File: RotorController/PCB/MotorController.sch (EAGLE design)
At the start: 18 parts

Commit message: Added thermal warning logic and fixed some layout issues.
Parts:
- removed D1: (no value), SparkFun-LED:LED-3MM-NO_SILK
- removed U1: (no value), SparkFun-IC-Power:V_REG_78XX-TO-220
- added IC1: 74ALS02N, 74xx-us:74ALS02N
- added J1: Waring LED, SparkFun-Connectors:CONN_02
- added J2: Power LED, SparkFun-Connectors:CONN_02
- added R10, R8: 2.2K, SparkFun-Resistors:RESISTORAXIAL-0.3
- added R6: 1K, SparkFun-Resistors:RESISTORAXIAL-0.3
- added R7, R9: 3.3K, SparkFun-Resistors:RESISTORAXIAL-0.3
- added U2: 5V, SparkFun-IC-Power:V_REG_78XXSINK
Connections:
- new net AZFLAG: AZHBRIDGE.THERMAL, R7.2
- new net ELFLAG: ELHBRIDGE.THERMAL, R9.2
- new net N$3: IC1D.I1, R10.2, R9.1
- new net N$5: J1.1, R6.2
- new net N$7: IC1D.I0, R7.1, R8.2
- new net WARNINGFLAG: IC1D.O, R6.1, UC1.A0
- net GND: now also IC1A.I0, IC1A.I1, IC1B.I0, IC1B.I1, IC1C.I0, IC1C.I1, IC1P.GND, J1.2, J2.2, R10.1, R8.1, U2.GND; no longer D1.C, U1.GND
- net N$8: now also J2.1; no longer D1.A
- net VCC: now also IC1P.VCC, U2.OUT; no longer U1.OUT
- net VCC_2: now also U2.IN; no longer U1.IN

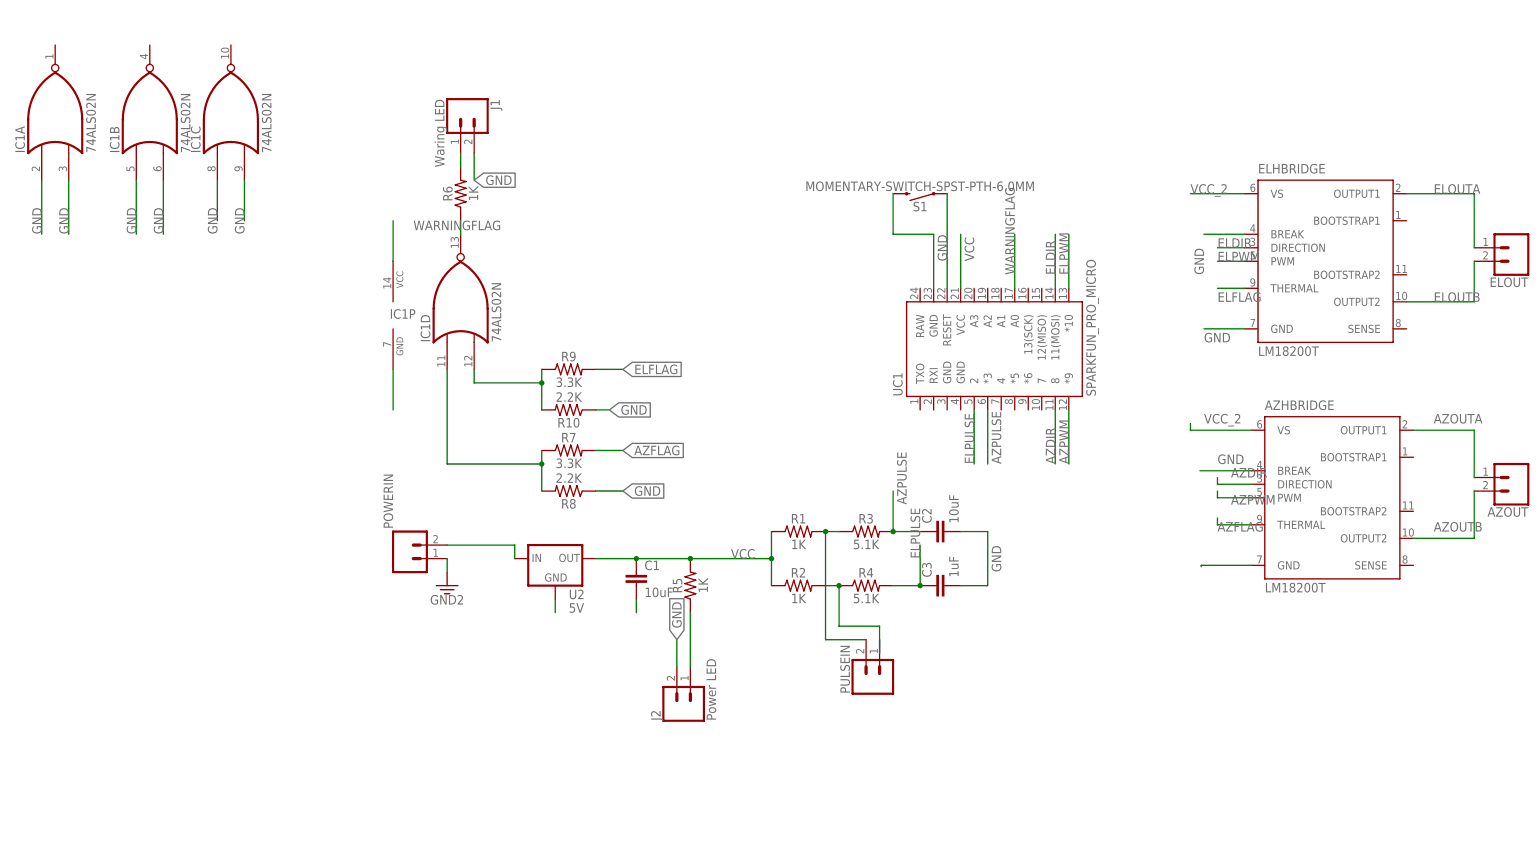
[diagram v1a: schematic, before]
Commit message: Fixed PCB files with accurate footprints for passive components. Included gerber files. Updated the arduino project layout.
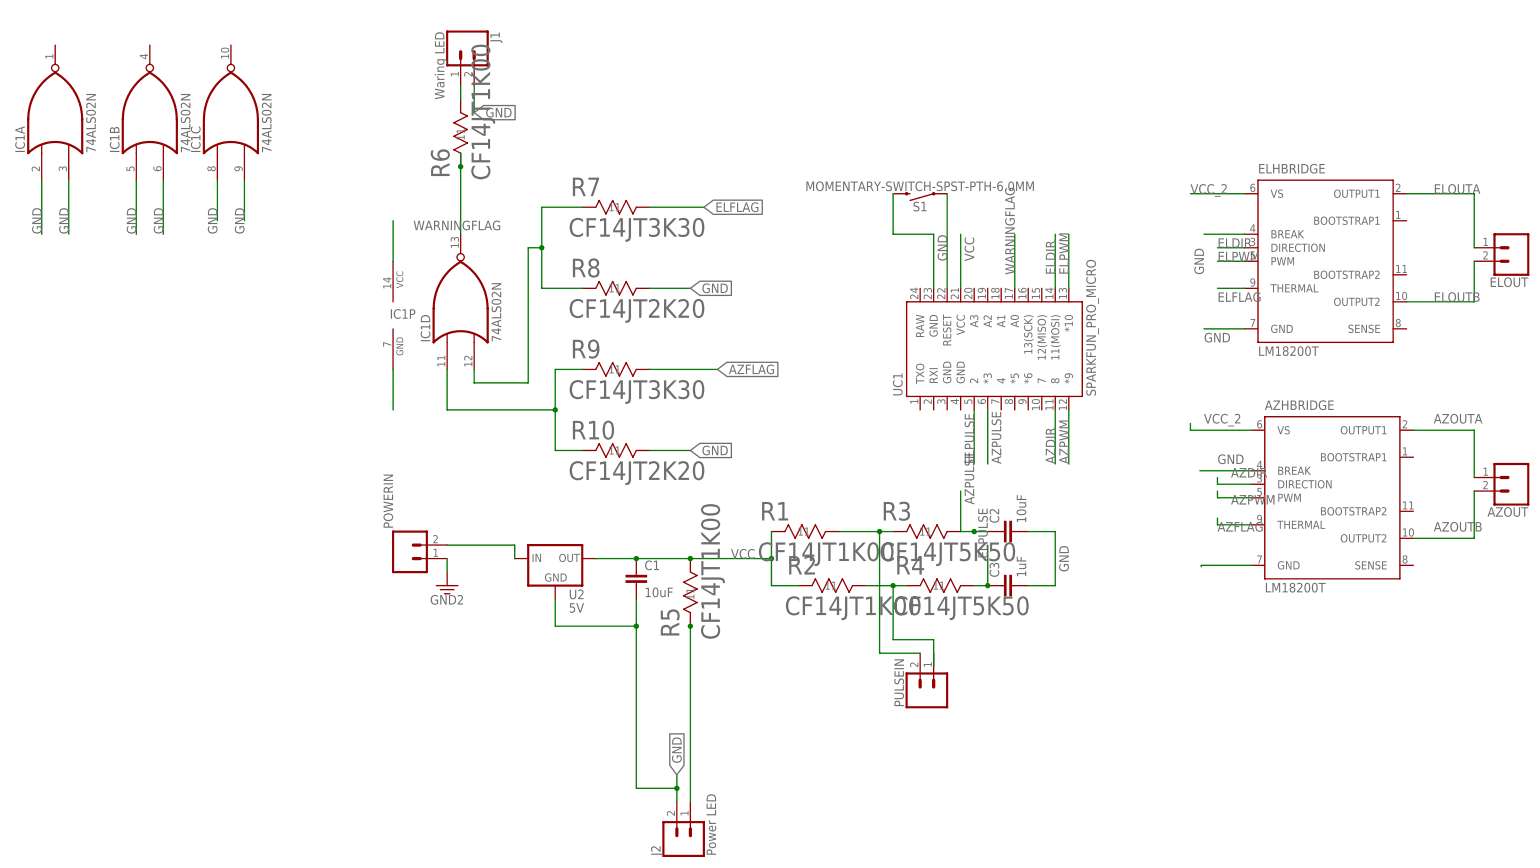
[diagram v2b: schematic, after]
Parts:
- R1, R2, R5, R6: value 1K -> CF14JT1K00; device SparkFun-Resistors:RESISTORAXIAL-0.3 -> DigiKeyImports:CF14JT1K00
- R10, R8: value 2.2K -> CF14JT2K20; device SparkFun-Resistors:RESISTORAXIAL-0.3 -> DigiKeyImports:CF14JT1K00
- R3, R4: value 5.1K -> CF14JT5K50; device SparkFun-Resistors:RESISTORAXIAL-0.3 -> DigiKeyImports:CF14JT1K00
- R7, R9: value 3.3K -> CF14JT3K30; device SparkFun-Resistors:RESISTORAXIAL-0.3 -> DigiKeyImports:CF14JT1K00
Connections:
- removed net N$7: IC1D.I0, R7.1, R8.2
- new net N$9: IC1D.I0, R10.11, R9.11
- net AZFLAG: now also R9.22; no longer R7.2
- net AZPULSE: now also R3.22; no longer R3.2
- net ELFLAG: now also R7.22; no longer R9.2
- net ELPULSE: now also R4.22; no longer R4.2
- net GND: now also R10.22, R8.22; no longer R10.1, R8.1
- net N$2: now also R1.22, R3.11; no longer R1.2, R3.1
- net N$3: now also R7.11, R8.11; no longer R10.2, R9.1
- net N$4: now also R2.22, R4.11; no longer R2.2, R4.1
- net N$5: now also R6.22; no longer R6.2
- net N$8: now also R5.11; no longer R5.1
- net VCC: now also R1.11, R2.11, R5.22; no longer R1.1, R2.1, R5.2
- net WARNINGFLAG: now also R6.11; no longer R6.1
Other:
- moved on the sheet: C2, C3, J1, J2, PULSEIN
